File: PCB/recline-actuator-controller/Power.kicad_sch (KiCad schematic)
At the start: 8 parts, among them J4 1757242, M1 D24V22F5, M2 D24V22F3

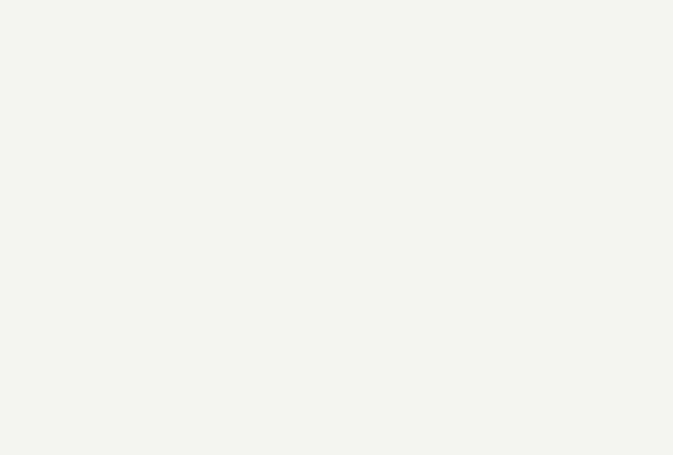
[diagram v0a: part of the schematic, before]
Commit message: PCB Layout Progress
Lots of progress made on PCB layout, MOSFET section complete, H-Bridges in progress, lots of work done and lots more to do, 3 copper layers are being utilized to provide ample copper for carrying all the current through he drivers and actuators.
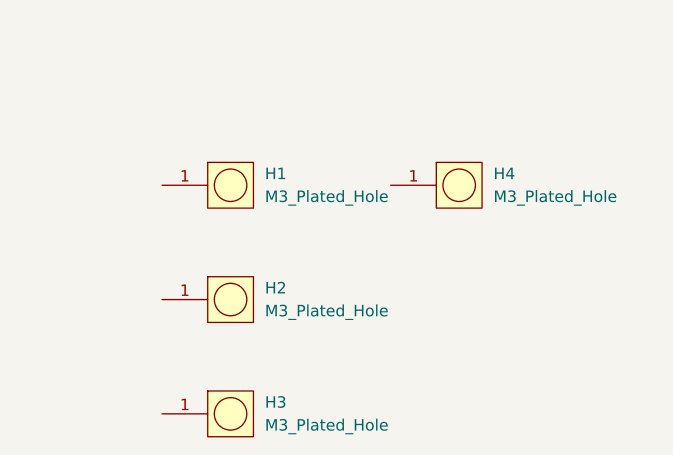
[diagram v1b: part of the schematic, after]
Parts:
- added H1, H2, H3, H4: M3_Plated_Hole, AVR-KiCAD-Lib-Holes_Fasteners:M3_HOLE, symbol AVR-KiCAD-Lib-Holes_Fasteners:M3_Plated_Hole

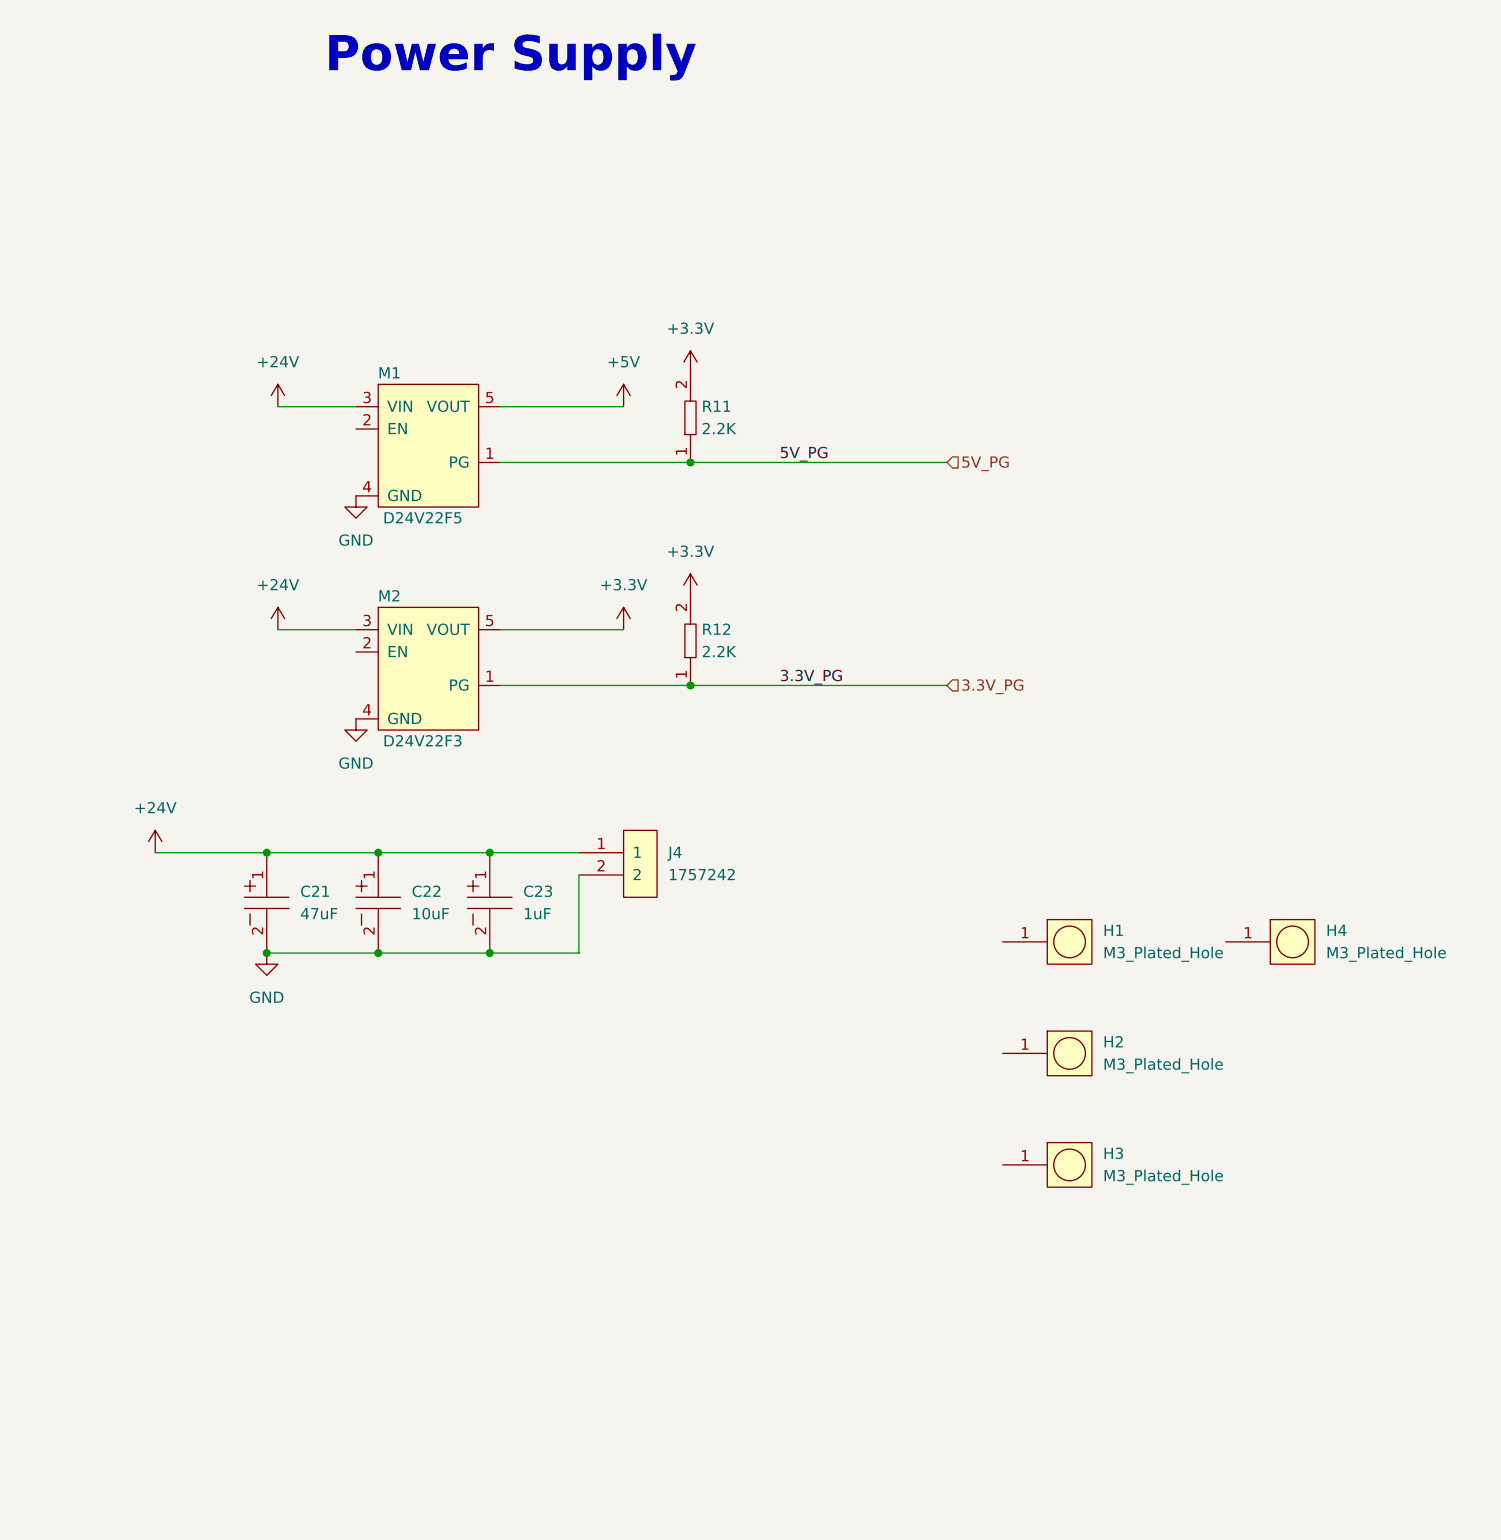
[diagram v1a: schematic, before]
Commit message: All Hardware Tweaked / 3D Renders
PCBs for Actuator Control, Recline Control HID, and 7 Segment carrier are all complete with full 3D models rendering. 3D Renders of all board added to repository img directory.
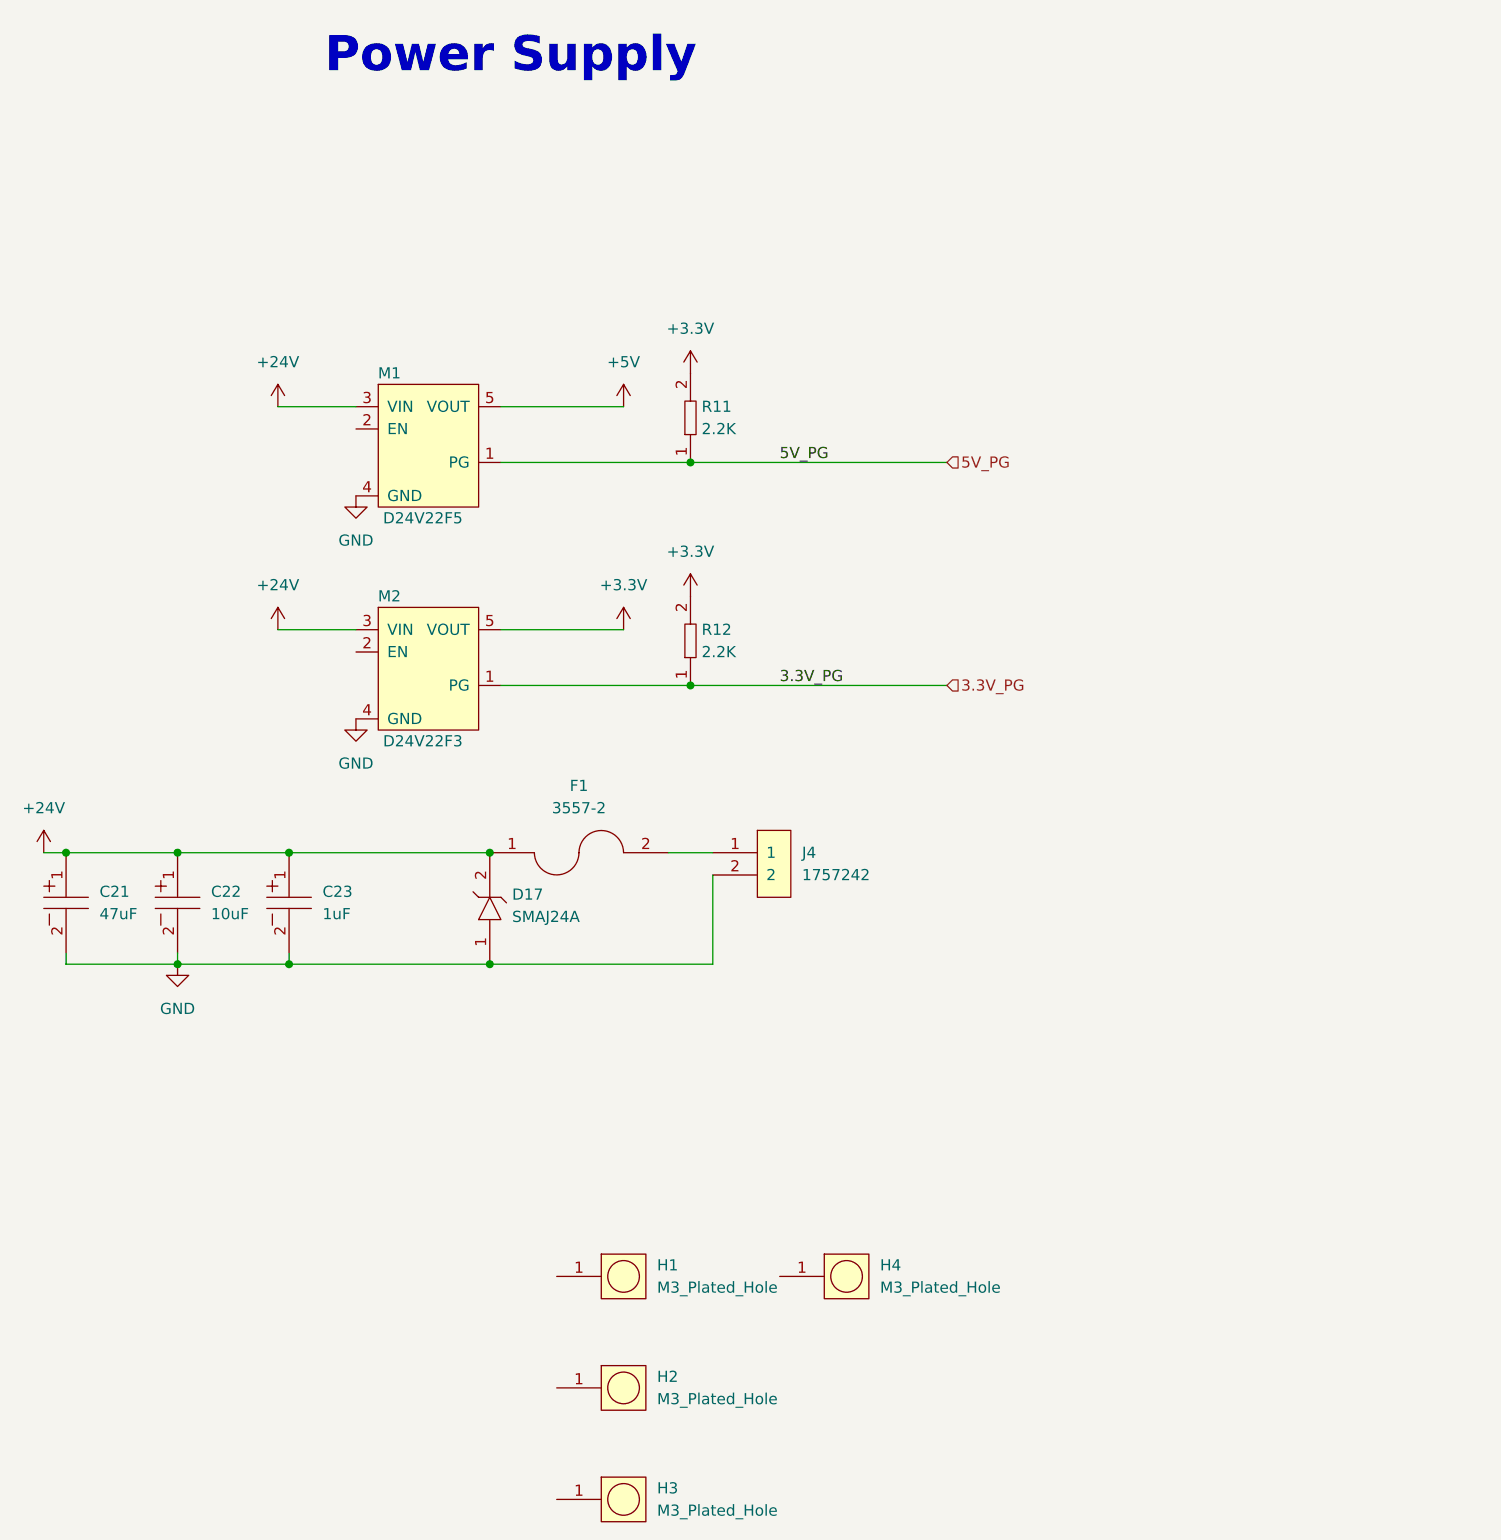
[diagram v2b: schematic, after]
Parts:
- added D17: SMAJ24A, AVR-KiCAD-Lib-Diodes:SMAJ, symbol AVR-KiCAD-Lib-Diodes:SMAJ24A
- added F1: 3557-2, AVR-KiCAD-Lib-Fuse-Holders:FUSE_3557-2, symbol AVR-KiCAD-Lib-Fuse-Holders:3557-2
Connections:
- net +24V: now also D17.2, F1.1; no longer J4.1
- net GND: now also D17.1
- new net: F1.2, J4.1
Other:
- moved on the sheet: C21, C22, C23, H1, H2, H3, H4, J4

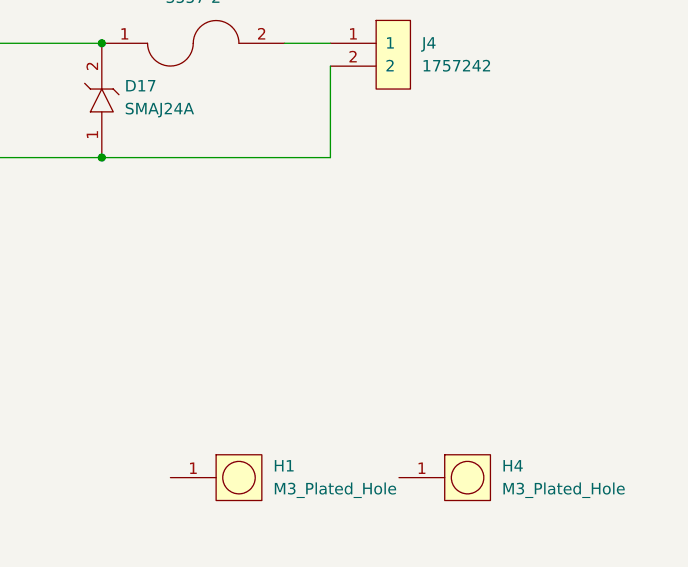
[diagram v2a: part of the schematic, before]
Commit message: Recline Actuator Board Redesign
Recline actuator control board redesign complete, functionality extended to handle two additional large actuators for leg lifting. Air compressor switching circuit made to handle higher current. Additional end stops for additional actuators added, IO expander added for more input to RP2040. Current sensing for all 4 actuators.
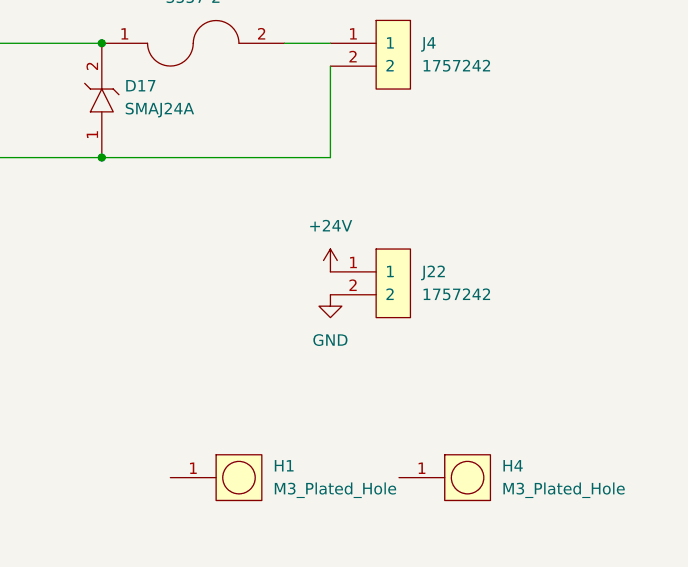
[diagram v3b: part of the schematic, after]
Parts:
- added J22: 1757242, AVR-KiCAD-Lib-Connectors:PhoenixContact_MSTBA-G_02x5.08mm_Angled, symbol AVR-KiCAD-Lib-Connectors:1757242
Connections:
- net +24V: now also J22.1
- net GND: now also J22.2

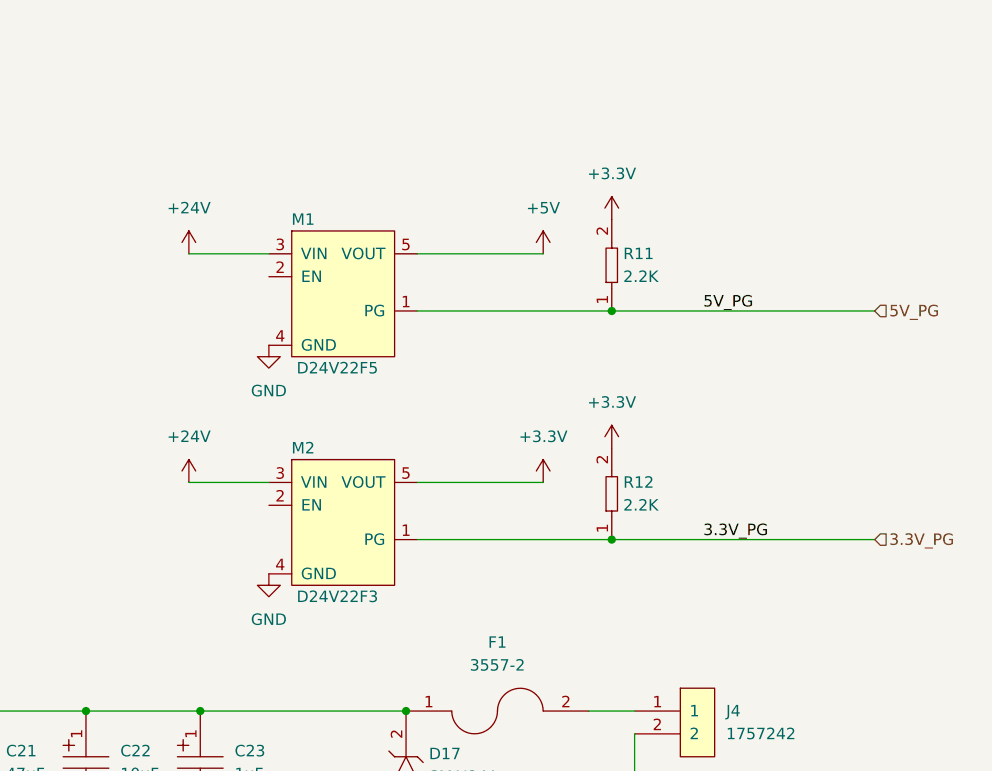
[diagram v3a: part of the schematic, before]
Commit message: RS485
RS485 schematic corrected, 5V regulator removed.
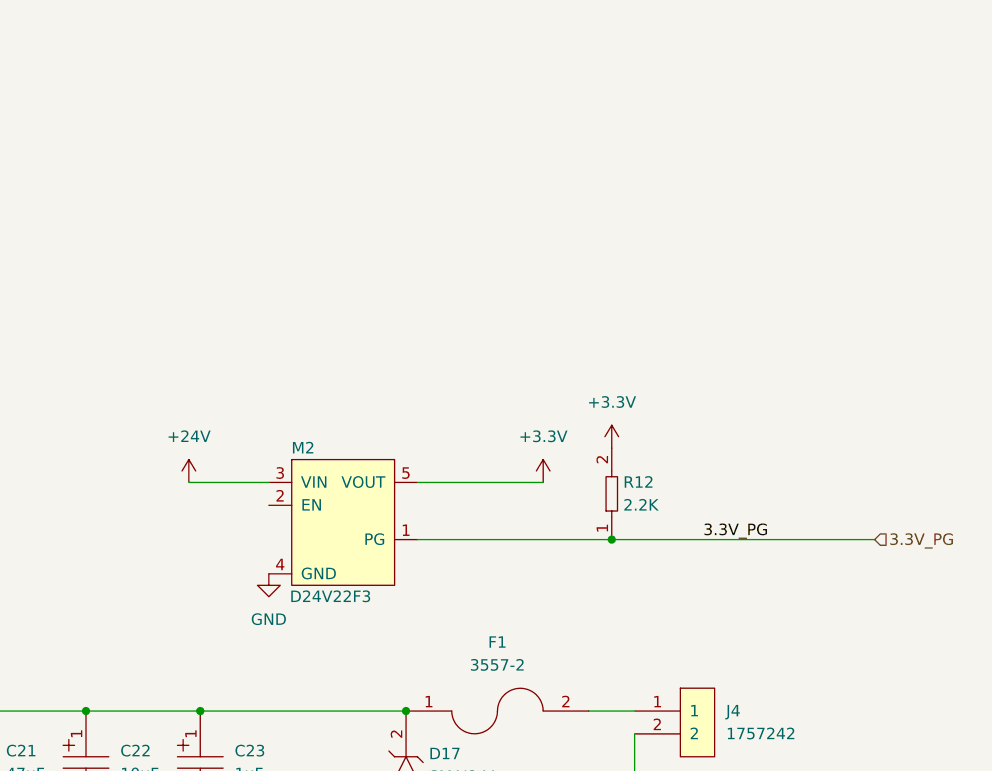
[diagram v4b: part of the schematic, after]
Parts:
- removed M1: D24V22F5, AVR-KiCAD-Lib-Modules:D24V22F12, symbol AVR-KiCAD-Lib-Modules:D24V22F5
- removed R11: RC0603FR-072K2L, AVR-KiCAD-Lib-Resistors:R0603, symbol AVR-KiCAD-Lib-Resistors:RC0603FR-072K2L

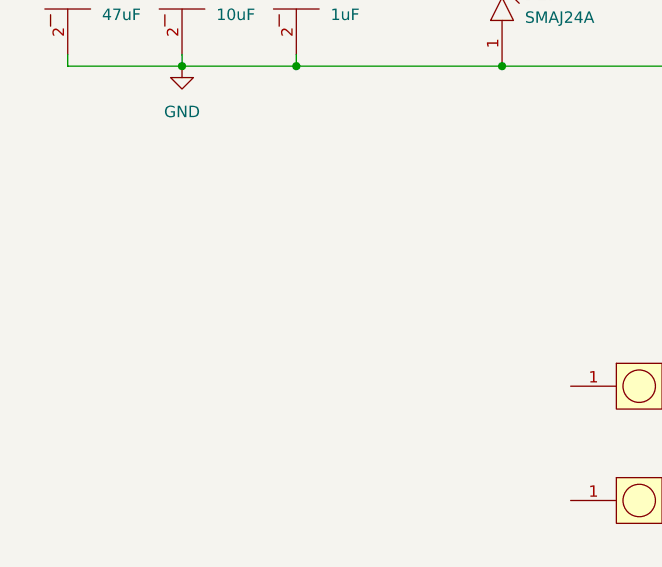
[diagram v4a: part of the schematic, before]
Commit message: Via Stichign and Pullups
Added optional pullups to endstop circuit.  Revised via stitching for input power, revised layout with added via stitching and copper pours for solenoid mosfets.
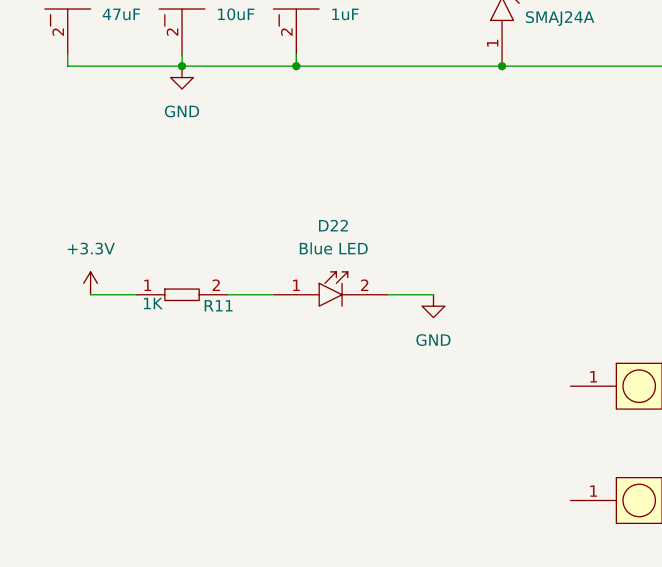
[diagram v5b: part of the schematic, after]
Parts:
- added D22: LTST-C194TBKT, AVR-KiCAD-Lib-Diodes:LED0603, symbol AVR-KiCAD-Lib-Diodes:LTST-C194TBKT
- added R11: RC0402FR-071KL, AVR-KiCAD-Lib-Resistors:R0402, symbol AVR-KiCAD-Lib-Resistors:RC0402FR-071KL
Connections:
- net +3.3V: now also R11.1
- net GND: now also D22.2
- new net: D22.1, R11.2
